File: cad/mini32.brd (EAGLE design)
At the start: 64 x 35 mm, 55 parts, among them CN1 MICROSDPLAIN, J1 HEADER-5X1, Q1 MOSFETSOT-23, SW2 SWITCHKMR211, SW3 SWITCHKMR211, U1 STM32F411/48, U2 LSM303D, U3 ADP5062, U4 MCP1824, U5 MAX17048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

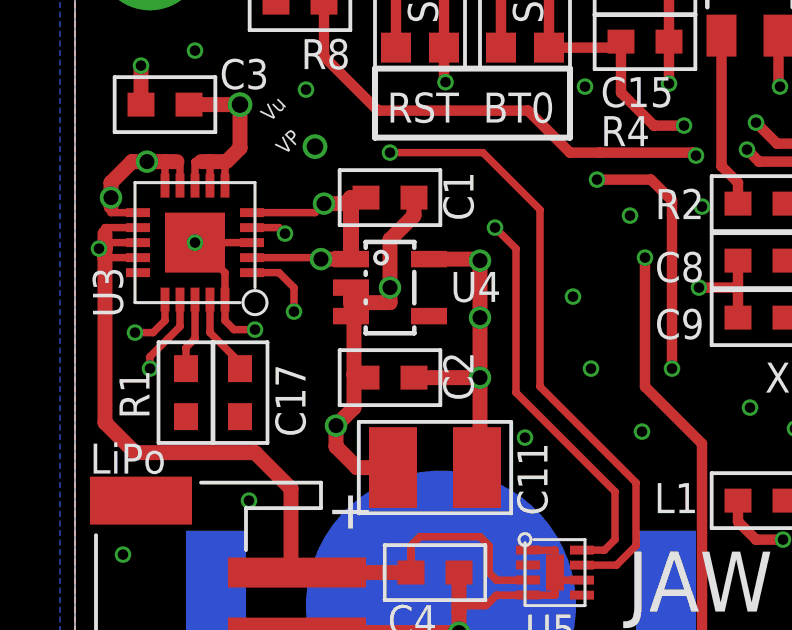
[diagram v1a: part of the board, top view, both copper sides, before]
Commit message: fix vreg
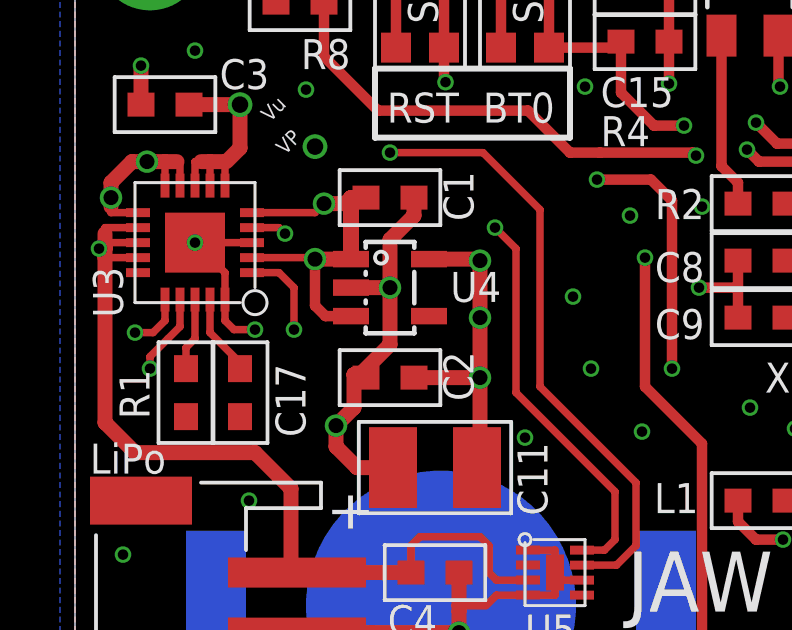
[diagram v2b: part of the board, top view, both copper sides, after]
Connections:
- net GND: no longer U4.3
- net VP: now also U4.3
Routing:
- net VP: track 19.6 -> 22.8 mm
- net I2CCL: track 110.6 -> 111.4 mm

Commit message: silk text
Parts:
- U$1, U$4: value ROBOTMAN-LOGO -> ROBOTMAN-LOGO2; device jaw:ROBOTMAN-LOGO -> jaw:ROBOTMAN-LOGO2
- moved U$1 1.14 mm to (42.9, 18.3)
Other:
- board text added: "AMIKETO"
- board text added: "AMIKETO Rev. 1"
- board text added: "JAW 2015-04"
- board text added: "www.amiketo.com"
- board text removed: "JAW mini32/11"
- board text removed: "mini32/11 Rev. 0"
- board text removed: "www.791RL.com"
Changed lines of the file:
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@@
 <grid distance="0.1" unitdist="mm" unit="mm" style="lines" multiple="5" display="yes" altdistance="0.025" altunitdist="inch" altunit="inch"/>
 <layers>
-<layer number="1" name="Top" color="4" fill="1" visible="yes" active="yes"/>
+<layer number="1" name="Top" color="4" fill="1" visible="no" active="yes"/>
 <layer number="2" name="V" color="5" fill="1" visible="no" active="yes"/>
 <layer number="3" name="Route3" color="4" fill="3" visible="no" active="no"/>
 <layer number="14" name="Route14" color="1" fill="6" visible="no" active="no"/>
-<layer number="15" name="Signal" color="1" fill="1" visible="yes" active="yes"/>
+<layer number="15" name="Signal" color="1" fill="1" visible="no" active="yes"/>
 <layer number="16" name="Bottom" color="6" fill="1" visible="no" active="yes"/>
 <layer number="17" name="Pads" color="2" fill="1" visible="yes" active="yes"/>
@@
 <layer number="19" name="Unrouted" color="6" fill="1" visible="yes" active="yes"/>
 <layer number="20" name="Dimension" color="15" fill="1" visible="yes" active="yes"/>
-<layer number="21" name="tPlace" color="7" fill="1" visible="yes" active="yes"/>
-<layer number="22" name="bPlace" color="7" fill="1" visible="no" active="yes"/>
+<layer number="21" name="tPlace" color="7" fill="1" visible="no" active="yes"/>
+<layer number="22" name="bPlace" color="7" fill="1" visible="yes" active="yes"/>
 <layer number="23" name="tOrigins" color="15" fill="1" visible="yes" active="yes"/>
 <layer number="24" name="bOrigins" color="15" fill="1" visible="yes" active="yes"/>
@@
 <text x="50.165" y="4" size="1" layer="21" ratio="10" rot="R90">MOSI</text>
 <text x="52.705" y="4" size="1" layer="21" ratio="10" rot="R90">MISO</text>
-<text x="60.5" y="16" size="2.45" layer="22" ratio="10" rot="MR0">JAW 2015-03</text>
-<text x="60.5" y="13" size="2.25" layer="22" ratio="10" rot="MR0">www.791RL.com</text>
-<text x="60.5" y="10" size="1.8" layer="22" ratio="10" rot="MR0">mini32/11 Rev. 0</text>
-<text x="4.5" y="34.5" size="1.25" layer="16" ratio="10" rot="MR180">JAW 2015-03</text>
-<text x="4.5" y="34.5" size="1.25" layer="30" ratio="10" rot="MR180">JAW 2015-03</text>
+<text x="60.5" y="16" size="2.45" layer="22" ratio="10" rot="MR0">JAW 2015-04</text>
+<text x="60.5" y="13" size="2.1" layer="22" ratio="10" rot="MR0">www.amiketo.com</text>
+<text x="60.5" y="10" size="2.1" layer="22" ratio="10" rot="MR0">AMIKETO Rev. 1</text>
+<text x="4.5" y="34.5" size="1.25" layer="16" ratio="15" rot="MR180">JAW 2015-03</text>
+<text x="4.5" y="34.5" size="1.25" layer="30" ratio="15" rot="MR180">JAW 2015-03</text>
 <text x="15.5" y="16.2" size="0.95" layer="22" ratio="10" rot="MR0">battery - CR1216</text>
 <text x="0.889" y="4" size="1" layer="22" ratio="10" rot="MR90">A0</text>
@@
 <circle x="47.4" y="22.2" radius="3.001665625" width="0.35" layer="22"/>
 <wire x1="49.5" y1="24.3" x2="45.3" y2="20.1" width="0.35" layer="22"/>
-<text x="18.4" y="7.7" size="2" layer="21" ratio="10">JAW
-mini32/11</text>
+<text x="17" y="7.4" size="2.5" layer="21" ratio="10">AMIKETO</text>
 <text x="10.4" y="27" size="1" layer="21" ratio="15">RST</text>
 <text x="13.6" y="27" size="1" layer="21" ratio="15">BT0</text>
@@
 <attribute name="VALUE" x="3.014" y="19.478" size="1" layer="27" font="vector" ratio="10" rot="R270"/>
 </element>
-<element name="U$4" library="jaw" package="ROBOTMAN-LOGO" value="ROBOTMAN-LOGO" x="56" y="23.1" rot="MR0"/>
+<element name="U$4" library="jaw" package="ROBOTMAN-LOGO2" value="ROBOTMAN-LOGO2" x="56" y="23.1" rot="MR0"/>
 <element name="B1" library="jaw" package="CR1216" value="BATTERY-CR2016" x="12.2" y="10.9" rot="MR0"/>
 <element name="X1" library="jaw" package="RESONATOR-CSTCE" value="12MHz" x="26.5" y="17.7" smashed="yes">
@@
 </element>
 <element name="LOGO1" library="Sparkfun-Aesthetics" package="OSHW-LOGO-M" value="OSHW-LOGOM" x="39.4" y="21.7" rot="MR0"/>
-<element name="U$1" library="jaw" package="ROBOTMAN-LOGO" value="ROBOTMAN-LOGO" x="44" y="18.6"/>
+<element name="U$1" library="jaw" package="ROBOTMAN-LOGO2" value="ROBOTMAN-LOGO2" x="42.9" y="18.3"/>
 <element name="R2" library="jaw" package="SMD0603" value="100" x="22.9" y="24.3" smashed="yes" rot="R180">
 <attribute name="NAME" x="20.978" y="24.784" size="1" layer="25" font="vector" ratio="10" rot="R180"/>
@@
 <via x="21.6" y="6.5" extent="1-16" drill="0.35"/>
 <via x="18.8" y="6.8" extent="1-16" drill="0.35"/>
-<via x="17.8" y="9" extent="1-16" drill="0.35"/>
+<via x="18.8" y="10" extent="1-16" drill="0.35"/>
 <via x="10.2" y="4.6" extent="1-16" drill="0.35"/>
 <via x="7.7" y="6.3" extent="1-16" drill="0.35"/>
@@
 <wire x1="15.1" y1="12.75" x2="15" y2="16.5" width="0" layer="19" extent="1-1"/>
 <wire x1="12.2" y1="10.9" x2="12.8" y2="10.9" width="0" layer="19" extent="1-16"/>
-<wire x1="17.8" y1="9" x2="16" y2="11.25" width="0" layer="19" extent="1-1"/>
-<wire x1="18.8" y1="6.8" x2="17.8" y2="9" width="0" layer="19" extent="1-1"/>
+<wire x1="18.8" y1="10" x2="16" y2="11.25" width="0" layer="19" extent="1-1"/>
+<wire x1="18.8" y1="6.8" x2="18.8" y2="10" width="0" layer="19" extent="1-1"/>
 <wire x1="21.6" y1="6.5" x2="18.8" y2="6.8" width="0" layer="19" extent="1-1"/>
 <wire x1="24.5" y1="6.6" x2="21.6" y2="6.5" width="0" layer="19" extent="1-1"/>
@@
 </board>
 </drawing>
-<compatibility>
-<note version="6.3" minversion="6.2.2" severity="warning">
-Since Version 6.2.2 text objects can contain more than one line,
-which will not be processed correctly with this version.
-</note>
-</compatibility>
 </eagle>

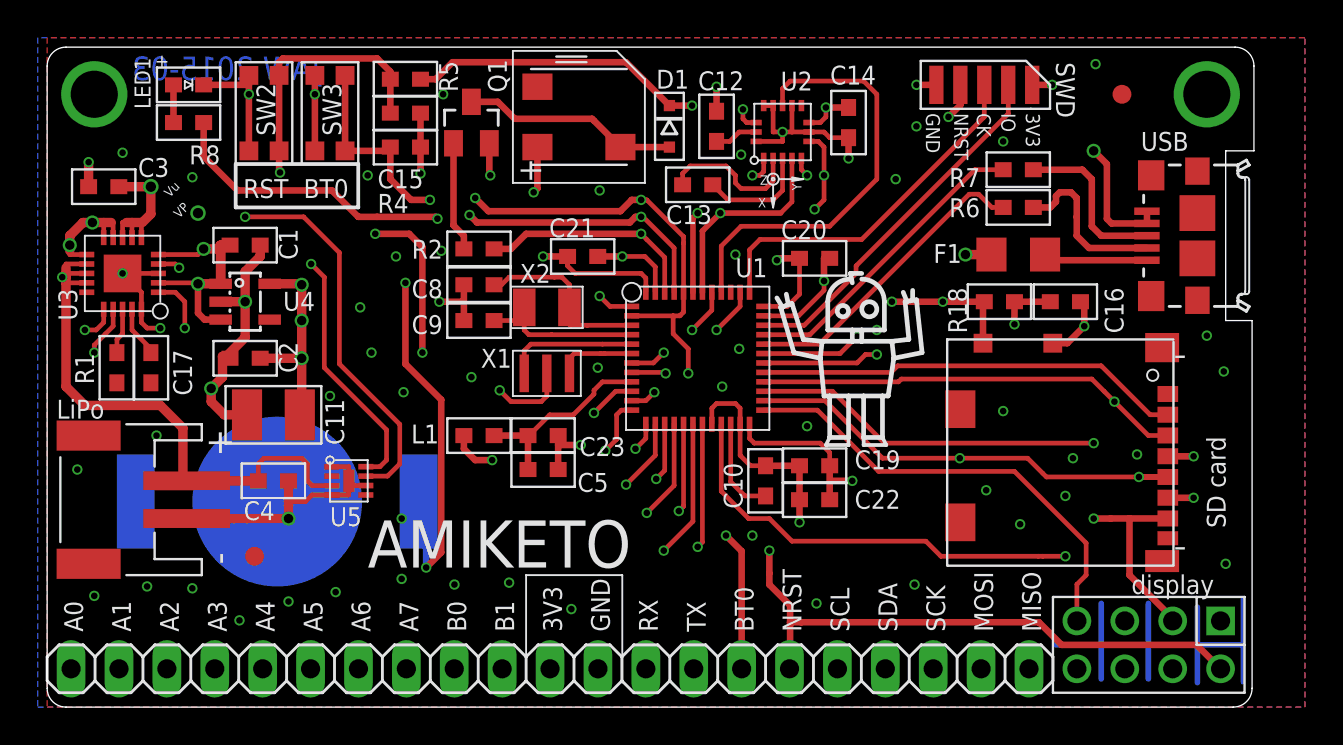
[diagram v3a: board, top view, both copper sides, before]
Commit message: add p-mosfet on sd+dpy power
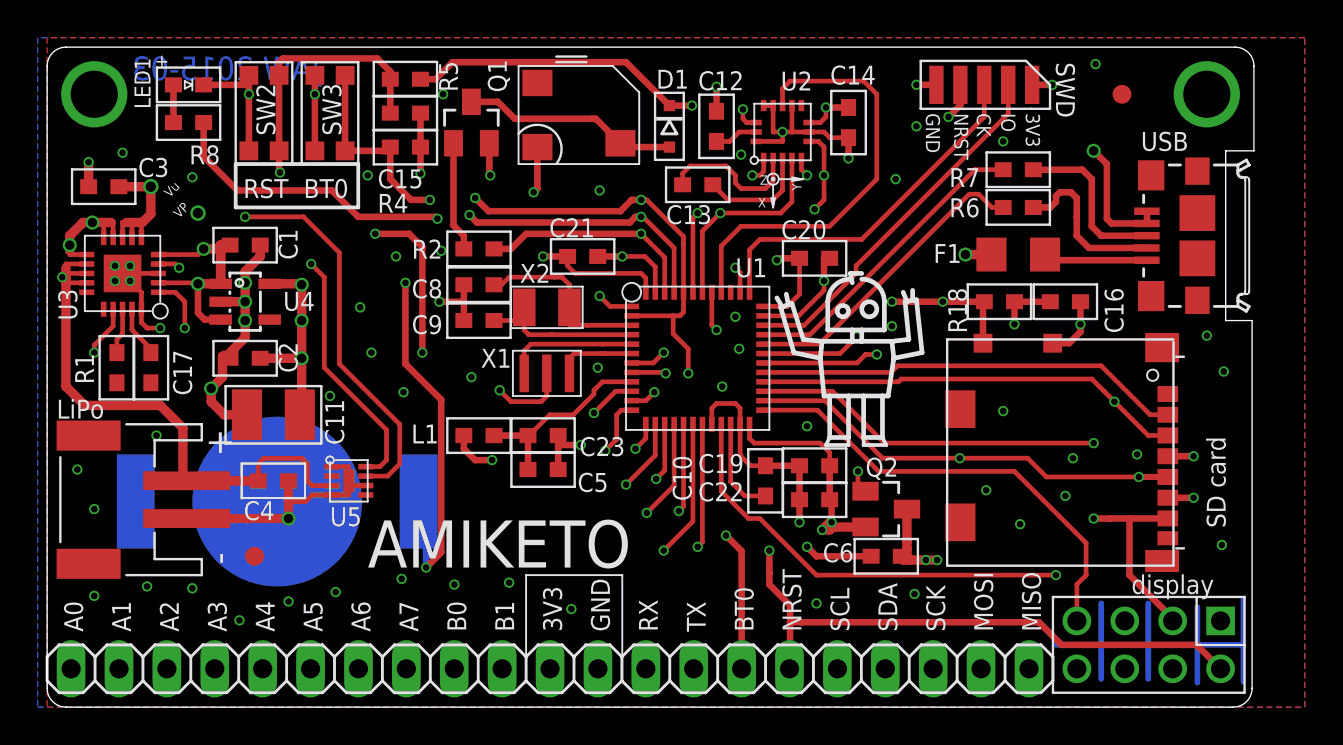
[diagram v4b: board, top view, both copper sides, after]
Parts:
- added C6: 1u, jaw:SMD0603
- added Q2: DMP2035U-7, jaw:SOT-23
- L1: value 40u -> 10u
- LED1: value LED -> white
- Q1: value MOSFETSOT-23 -> IRLML6344TRPBF
- R18: value 10k -> 100k
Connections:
- new net NPWREN: Q2.1, U1.P41
- new net VCCE: C16.1, C6.1, CN1.4, CN1.SW1, CN6.1, Q2.3
- net BATSTAT: no longer U1.P41
- net GND: now also C6.2
- net VCC: now also Q2.2; no longer C16.1, CN1.4, CN1.SW1, CN6.1
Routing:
- net BATSTAT: track 39.6 -> 0.00 mm, vias 2 -> 0
- net NPWREN: track 0.00 -> 16.8 mm, vias 0 -> 2
- net VCCE: track 0.00 -> 9.50 mm, vias 0 -> 4
- net GND: track 131.9 -> 134.8 mm, vias 74 -> 79
- net N$21: track 34.6 -> 32.1 mm
- net IOCARD: track 19.6 -> 17.6 mm
- net VCC: track 69.6 -> 67.7 mm, vias 16 -> 15
- net DPYDC: track 31.2 -> 30.6 mm
- added copper zone on layer 2, net VCCE

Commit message: move vias
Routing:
- net BOOT0: track 52.6 -> 59.8 mm, vias 5 -> 4
- net NPWREN: track 16.8 -> 21.6 mm
- net NRST: track 131.9 -> 128.7 mm
- net IOA1: track 41.5 -> 39.0 mm
- net IMUINT: track 23.0 -> 22.5 mm
- net IOB1: track 21.1 -> 21.7 mm

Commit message: cap on vbat
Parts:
- added C7: 1u, jaw:SMD0603
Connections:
- net GND: now also C7.1
- net N$21: now also C7.2
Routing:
- net N$21: track 32.1 -> 34.7 mm
- net GND: track 134.8 -> 137.3 mm
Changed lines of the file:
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@@
 <element name="B1" library="jaw" package="CR1216" value="BATTERY-CR2016" x="12.2" y="10.9" rot="MR0"/>
 <element name="X1" library="jaw" package="RESONATOR-CSTCE" value="12MHz" x="26.5" y="17.7" smashed="yes">
-<attribute name="NAME" x="23" y="18" size="1" layer="25" ratio="10"/>
+<attribute name="NAME" x="23.2" y="16.5" size="1" layer="25" ratio="10"/>
 </element>
 <element name="U2" library="jaw" package="LGA16A" value="LSM303D" x="39" y="30.5" smashed="yes">
@@
 <attribute name="NAME" x="42.778" y="8.684" size="1" layer="25" font="vector" ratio="10" rot="R180"/>
 <attribute name="VALUE" x="46.278" y="10.086" size="1" layer="27" font="vector" ratio="10" rot="R180"/>
+</element>
+<element name="C7" library="jaw" package="SMD0603" value="1u" x="22.9" y="18.7" smashed="yes" rot="R180">
+<attribute name="NAME" x="20.978" y="19.184" size="1" layer="25" font="vector" ratio="10" rot="R180"/>
+<attribute name="VALUE" x="24.678" y="20.786" size="1" layer="27" font="vector" ratio="10" rot="R180"/>
 </element>
 </elements>
@@
 <via x="40.3" y="14.9" extent="1-16" drill="0.35"/>
 <via x="12.8" y="5.6" extent="1-16" drill="0.35"/>
-<via x="22.5" y="17.5" extent="1-16" drill="0.35"/>
+<via x="22.3" y="16.8" extent="1-16" drill="0.35"/>
 <via x="1.6" y="12.6" extent="1-16" drill="0.35"/>
 <via x="2.5" y="5.9" extent="1-16" drill="0.35"/>
@@
 <wire x1="43.7" y1="8" x2="40.8" y2="8" width="0.35" layer="1"/>
 <wire x1="40.8" y1="8" x2="40.3" y2="8.5" width="0.35" layer="1"/>
+<contactref element="C7" pad="1"/>
+<wire x1="23.7" y1="18.7" x2="23.7" y2="18.2" width="0.35" layer="1"/>
+<wire x1="23.7" y1="18.2" x2="22.3" y2="16.8" width="0.35" layer="1"/>
 <wire x1="55.6" y1="34.1" x2="61.5" y2="32.5" width="0" layer="19" extent="1-1"/>
 <wire x1="55.5" y1="29.5" x2="55.6" y2="34.1" width="0" layer="19" extent="1-1"/>
@@
 <wire x1="35.5" y1="31.6" x2="38" y2="31.9" width="0" layer="19" extent="1-1"/>
 <wire x1="41.2" y1="23.8" x2="40.3" y2="28.2" width="0" layer="19" extent="1-1"/>
-<wire x1="36.5" y1="18.9" x2="38" y2="20.75" width="0" layer="19" extent="1-1"/>
+<wire x1="36.5" y1="20.7" x2="38" y2="20.75" width="0" layer="19" extent="1-1"/>
+<wire x1="36.5" y1="18.9" x2="36.5" y2="20.7" width="0" layer="19" extent="1-1"/>
 <wire x1="35.9" y1="17.2" x2="36.5" y2="18.9" width="0" layer="19" extent="1-1"/>
 <wire x1="35.5" y1="16.1" x2="35.9" y2="17.2" width="0" layer="19" extent="1-1"/>
@@
 <wire x1="40.3" y1="14.9" x2="39.9" y2="12.8" width="0" layer="19" extent="1-1"/>
 <wire x1="40.8" y1="5.5" x2="40.8" y2="8" width="0" layer="19" extent="1-1"/>
+<wire x1="46" y1="6" x2="43.7" y2="8" width="0" layer="19" extent="1-1"/>
 <wire x1="32.8" y1="17.7" x2="35.25" y2="15.85" width="0" layer="19" extent="1-1"/>
-<wire x1="32.8" y1="19.6" x2="31" y2="17.75" width="0" layer="19" extent="1-1"/>
-<wire x1="26.5" y1="17.7" x2="32.8" y2="19.6" width="0" layer="19" extent="1-1"/>
-<wire x1="22.5" y1="17.5" x2="24" y2="16.8" width="0" layer="19" extent="1-1"/>
+<wire x1="32.8" y1="19.6" x2="32.75" y2="17.75" width="0" layer="19" extent="1-1"/>
+<wire x1="32.25" y1="22" x2="32.8" y2="19.6" width="0" layer="19" extent="1-1"/>
+<wire x1="29.3" y1="27.4" x2="29.2" y2="23.9" width="0" layer="19" extent="1-1"/>
+<wire x1="44.8" y1="20.2" x2="41.2" y2="22.1" width="0" layer="19" extent="1-1"/>
+<wire x1="26.5" y1="17.7" x2="31" y2="17.75" width="0" layer="19" extent="1-1"/>
+<wire x1="23.7" y1="18.2" x2="24" y2="16.8" width="0" layer="19" extent="1-1"/>
 <wire x1="27.1" y1="14.4" x2="26.2" y2="16.2" width="0" layer="19" extent="1-1"/>
-<wire x1="22.1" y1="20.5" x2="22.5" y2="17.5" width="0" layer="19" extent="1-1"/>
+<wire x1="22.1" y1="20.5" x2="23.7" y2="18.7" width="0" layer="19" extent="1-1"/>
 <wire x1="20.9" y1="24.2" x2="22.1" y2="22.4" width="0" layer="19" extent="1-1"/>
 <wire x1="18.5" y1="23.9" x2="20.9" y2="24.2" width="0" layer="19" extent="1-1"/>
-<wire x1="46" y1="6" x2="43.7" y2="8" width="0" layer="19" extent="1-1"/>
 <wire x1="16.6" y1="21.2" x2="18.5" y2="23.9" width="0" layer="19" extent="1-1"/>
 <wire x1="17.2" y1="18.8" x2="16.6" y2="21.2" width="0" layer="19" extent="1-1"/>
 <wire x1="18.9" y1="16.7" x2="17.2" y2="18.8" width="0" layer="19" extent="1-1"/>
 <wire x1="15" y1="16.5" x2="17.2" y2="18.8" width="0" layer="19" extent="1-1"/>
-<wire x1="44.8" y1="20.2" x2="41.2" y2="22.1" width="0" layer="19" extent="1-1"/>
-<wire x1="36.5" y1="20.7" x2="38" y2="20.75" width="0" layer="19" extent="1-1"/>
 <wire x1="15.1" y1="12.75" x2="15" y2="16.5" width="0" layer="19" extent="1-1"/>
 <wire x1="12.2" y1="10.9" x2="12.8" y2="10.9" width="0" layer="19" extent="1-16"/>
@@
 <wire x1="17" y1="28.2" x2="19.8" y2="28.3" width="0" layer="19" extent="1-1"/>
 <wire x1="23.45" y1="29.9" x2="21" y2="32.5" width="0" layer="19" extent="1-1"/>
-<wire x1="32.25" y1="22" x2="32.75" y2="17.75" width="0" layer="19" extent="1-1"/>
-<wire x1="29.3" y1="27.4" x2="29.2" y2="23.9" width="0" layer="19" extent="1-1"/>
 <wire x1="2.2" y1="27.6" x2="3.6" y2="23.4" width="0" layer="19" extent="1-1"/>
 <wire x1="4" y1="29.4" x2="2.2" y2="28.9" width="0" layer="19" extent="1-1"/>
@@
 <via x="19" y="22.5" extent="1-16" drill="0.35"/>
 <wire x1="19" y1="22.5" x2="19" y2="18.2" width="0.35" layer="1"/>
-<wire x1="19" y1="18.2" x2="20.9" y2="16.3" width="0.35" layer="1"/>
+<wire x1="19" y1="18.2" x2="20.2" y2="17" width="0.35" layer="1"/>
+<wire x1="20.2" y1="17" x2="20.9" y2="16.3" width="0.35" layer="1"/>
 <wire x1="20.9" y1="16.3" x2="20.9" y2="8.2" width="0.35" layer="1"/>
 <wire x1="20.9" y1="8.2" x2="20.1" y2="7.4" width="0.35" layer="1"/>
 <via x="20.1" y="7.4" extent="1-16" drill="0.35"/>
 <wire x1="20.1" y1="7.4" x2="20.1" y2="10.8" width="0.35" layer="16"/>
-<wire x1="20.1" y1="10.8" x2="19.7" y2="10.9" width="0" layer="19" extent="1-16"/>
+<contactref element="C7" pad="2"/>
+<wire x1="22.1" y1="18.7" x2="21.9" y2="18.7" width="0.35" layer="1"/>
+<wire x1="21.9" y1="18.7" x2="20.2" y2="17" width="0.35" layer="1"/>
+<wire x1="20.1" y1="10.8" x2="19.7" y2="10.9" width="0" layer="19" extent="16-16"/>
 <wire x1="4.7" y1="10.9" x2="19.7" y2="10.9" width="0" layer="19" extent="16-16"/>
 </signal>

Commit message: ground pad
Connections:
- net GND: now also U1.PAD
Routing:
- net GND: track 137.3 -> 146.6 mm
- net BOOT0: track 59.8 -> 62.8 mm, vias 4 -> 5
